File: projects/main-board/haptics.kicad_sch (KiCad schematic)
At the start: 12 parts, among them M1 Motor_DC, M2 Motor_DC, Q1 Q_NPN_CBE, Q2 Q_NPN_CBE

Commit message: Updated schematics with new symbols
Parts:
- removed U11: ~, symbol symbol-library:TLV74330PDBVR
- added U7: TLV74330PDBVR, footprint-library:TLV74330PDBVR, symbol symbol-library:TLV74330PDBVR
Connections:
- net GND: now also U7.2 (GND)
- net MOTOR_PWR_EN: now also U7.3 (EN)
- net VSYS: now also U7.1 (IN)
- net at C101.1, C103.1, M1.1 (+)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: now also U7.5 (OUT)
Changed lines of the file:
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@@
-	)
-	(symbol
-		(lib_id "symbol-library:TLV74330PDBVR")
-		(at 104.14 74.93 0)
-		(unit 1)
-		(exclude_from_sim no)
-		(in_bom yes)
-		(on_board yes)
-		(dnp no)
-		(property "Reference" "U11"
-			(at 105.664 73.66 0)
-			(effects
-				(font
-					(size 1.27 1.27)
-				)
-			)
-		)
-		(property "Value" "~"
-			(at 109.474 73.406 0)
-			(effects
-				(font
-					(size 1.27 1.27)
-				)
-			)
-		)
-		(property "Footprint" ""
-			(at 104.14 74.93 0)
-			(effects
-				(font
-					(size 1.27 1.27)
-				)
-				(hide yes)
-			)
-		)
-		(property "Datasheet" ""
-			(at 104.14 74.93 0)
-			(effects
-				(font
-					(size 1.27 1.27)
-				)
-				(hide yes)
-			)
-		)
-		(property "Description" ""
-			(at 104.14 74.93 0)
-			(effects
-				(font
-					(size 1.27 1.27)
-				)
-				(hide yes)
-			)
-		)
-		(pin "3"
-		)
-		(pin "1"
-		)
-		(pin "5"
-		)
-		(pin "4"
-		)
-		(pin "2"
-		)
-		(instances
-			(project ""
-				(path "/c621b5fd-2ef7-4a67-960d-0ffc72b1245a/ad680993-3156-41a9-bb71-e4719f61fa1c"
-					(reference "U11")
-					(unit 1)
-				)
-			)
-		)
 	)
 	(symbol
@@
 					(unit 1)
 				)
+			)
+		)
+	)
+	(symbol
+		(lib_name "TLV74330PDBVR_1")
+		(lib_id "symbol-library:TLV74330PDBVR")
+		(at 104.14 74.93 0)
+		(unit 1)
+		(exclude_from_sim no)
+		(in_bom yes)
+		(on_board yes)
+		(dnp no)
+		(property "Reference" "U7"
+			(at 105.156 73.914 0)
+			(effects
+				(font
+					(size 1.27 1.27)
+				)
+			)
+		)
+		(property "Value" "TLV74330PDBVR"
+			(at 110.998 96.774 0)
+			(effects
+				(font
+					(size 1.27 1.27)
+				)
+			)
+		)
+		(property "Footprint" "footprint-library:TLV74330PDBVR"
+			(at 117.348 97.79 0)
+			(effects
+				(font
+					(size 1.27 1.27)
+				)
+				(hide yes)
+			)
+		)
+		(property "Datasheet" ""
+			(at 104.14 74.93 0)
+			(effects
+				(font
+					(size 1.27 1.27)
+				)
+				(hide yes)
+			)
+		)
+		(property "Description" ""
+			(at 104.14 74.93 0)
+			(effects
+				(font
+					(size 1.27 1.27)
+				)
+				(hide yes)
+			)
+		)
+		(pin "1"
+		)
+		(pin "3"
+		)
+		(pin "5"
+		)
+		(pin "4"
+		)
+		(pin "2"
+		)
+		(instances
+			(project ""
+				(path "/c621b5fd-2ef7-4a67-960d-0ffc72b1245a/ad680993-3156-41a9-bb71-e4719f61fa1c"
+					(reference "U7")
+					(unit 1)
+				)

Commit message: Re-annotate schematics.
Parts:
- renumbered C99 to C101, C101 to C102, R18 to R57, R14 to R58, R17 to R59, U7 to U12
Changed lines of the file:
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@@
 		(dnp no)
 		(fields_autoplaced yes)
-		(property "Reference" "#PWR0130"
+		(property "Reference" "#PWR0145"
 			(at 77.47 92.71 0)
 			(effects
@@
 			(project "main-board"
 				(path "/c621b5fd-2ef7-4a67-960d-0ffc72b1245a/ad680993-3156-41a9-bb71-e4719f61fa1c"
-					(reference "#PWR0130")
+					(reference "#PWR0145")
 					(unit 1)
 				)
@@
 		(dnp no)
 		(fields_autoplaced yes)
-		(property "Reference" "#PWR0128"
+		(property "Reference" "#PWR0144"
 			(at 77.47 80.01 0)
 			(effects
@@
 			(project ""
 				(path "/c621b5fd-2ef7-4a67-960d-0ffc72b1245a/ad680993-3156-41a9-bb71-e4719f61fa1c"
-					(reference "#PWR0128")
+					(reference "#PWR0144")
 					(unit 1)
 				)
@@
 		(on_board yes)
 		(dnp no)
-		(property "Reference" "R18"
+		(property "Reference" "R57"
 			(at 94.488 97.282 0)
 			(effects
@@
 			(project "main-board"
 				(path "/c621b5fd-2ef7-4a67-960d-0ffc72b1245a/ad680993-3156-41a9-bb71-e4719f61fa1c"
-					(reference "R18")
+					(reference "R57")
 					(unit 1)
 				)
@@
 		(dnp no)
 		(fields_autoplaced yes)
-		(property "Reference" "#PWR0133"
+		(property "Reference" "#PWR0146"
 			(at 97.79 132.08 0)
 			(effects
@@
 			(project "main-board"
 				(path "/c621b5fd-2ef7-4a67-960d-0ffc72b1245a/ad680993-3156-41a9-bb71-e4719f61fa1c"
-					(reference "#PWR0133")
+					(reference "#PWR0146")
 					(unit 1)
 				)
@@
 		(on_board yes)
 		(dnp no)
-		(property "Reference" "R14"
+		(property "Reference" "R58"
 			(at 152.654 105.664 90)
 			(effects
@@
 			(project ""
 				(path "/c621b5fd-2ef7-4a67-960d-0ffc72b1245a/ad680993-3156-41a9-bb71-e4719f61fa1c"
-					(reference "R14")
+					(reference "R58")
 					(unit 1)
 				)
@@
 		(dnp no)
 		(fields_autoplaced yes)
-		(property "Reference" "C99"
+		(property "Reference" "C101"
 			(at 92.71 80.0162 0)
 			(effects
@@
 			(project "main-board"
 				(path "/c621b5fd-2ef7-4a67-960d-0ffc72b1245a/ad680993-3156-41a9-bb71-e4719f61fa1c"
-					(reference "C99")
+					(reference "C101")
 					(unit 1)
 				)
@@
 		(dnp no)
 		(fields_autoplaced yes)
-		(property "Reference" "C101"
+		(property "Reference" "C102"
 			(at 134.62 80.0162 0)
 			(effects
@@
 			(project "main-board"
 				(path "/c621b5fd-2ef7-4a67-960d-0ffc72b1245a/ad680993-3156-41a9-bb71-e4719f61fa1c"
-					(reference "C101")
+					(reference "C102")
 					(unit 1)
 				)
@@
 		(on_board yes)
 		(dnp no)
-		(property "Reference" "R17"
+		(property "Reference" "R59"
 			(at 199.39 105.918 90)
 			(effects
@@
 			(project "main-board"
 				(path "/c621b5fd-2ef7-4a67-960d-0ffc72b1245a/ad680993-3156-41a9-bb71-e4719f61fa1c"
-					(reference "R17")
+					(reference "R59")
 					(unit 1)
 				)
@@
 		(on_board yes)
 		(dnp no)
-		(property "Reference" "U7"
+		(property "Reference" "U12"
 			(at 105.156 73.914 0)
 			(effects
@@
 			(project ""
 				(path "/c621b5fd-2ef7-4a67-960d-0ffc72b1245a/ad680993-3156-41a9-bb71-e4719f61fa1c"
-					(reference "U7")
-					(unit 1)
-				)
+					(reference "U12")
+					(unit 1)
+				)

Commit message: Normalise capacitors
- Add capacitor parts to library.
- Replace all placeholder capacitors
  with the actual part numbers.
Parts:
- removed C100, C102: 10uF 10V, symbol Device:C_Small
- removed C101, C103: 100nF 10V, symbol Device:C_Small
- added C100, C102: 10uF 10V, Capacitor_SMD:C_0603_1608Metric, symbol symbol-library-capacitors:CC0603MRX5R6BB106
- added C101, C103: 100nF 10V, Capacitor_SMD:C_0402_1005Metric, symbol symbol-library-capacitors:CC0402KRX7R6BB104
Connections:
- net GND: now also C100.2, C101.2, C102.2, C103.2
- net VSYS: now also C100.1, C101.1
- net at M1.1 (+), M2.1 (+), U12.5 (OUT): now also C102.1, C103.1

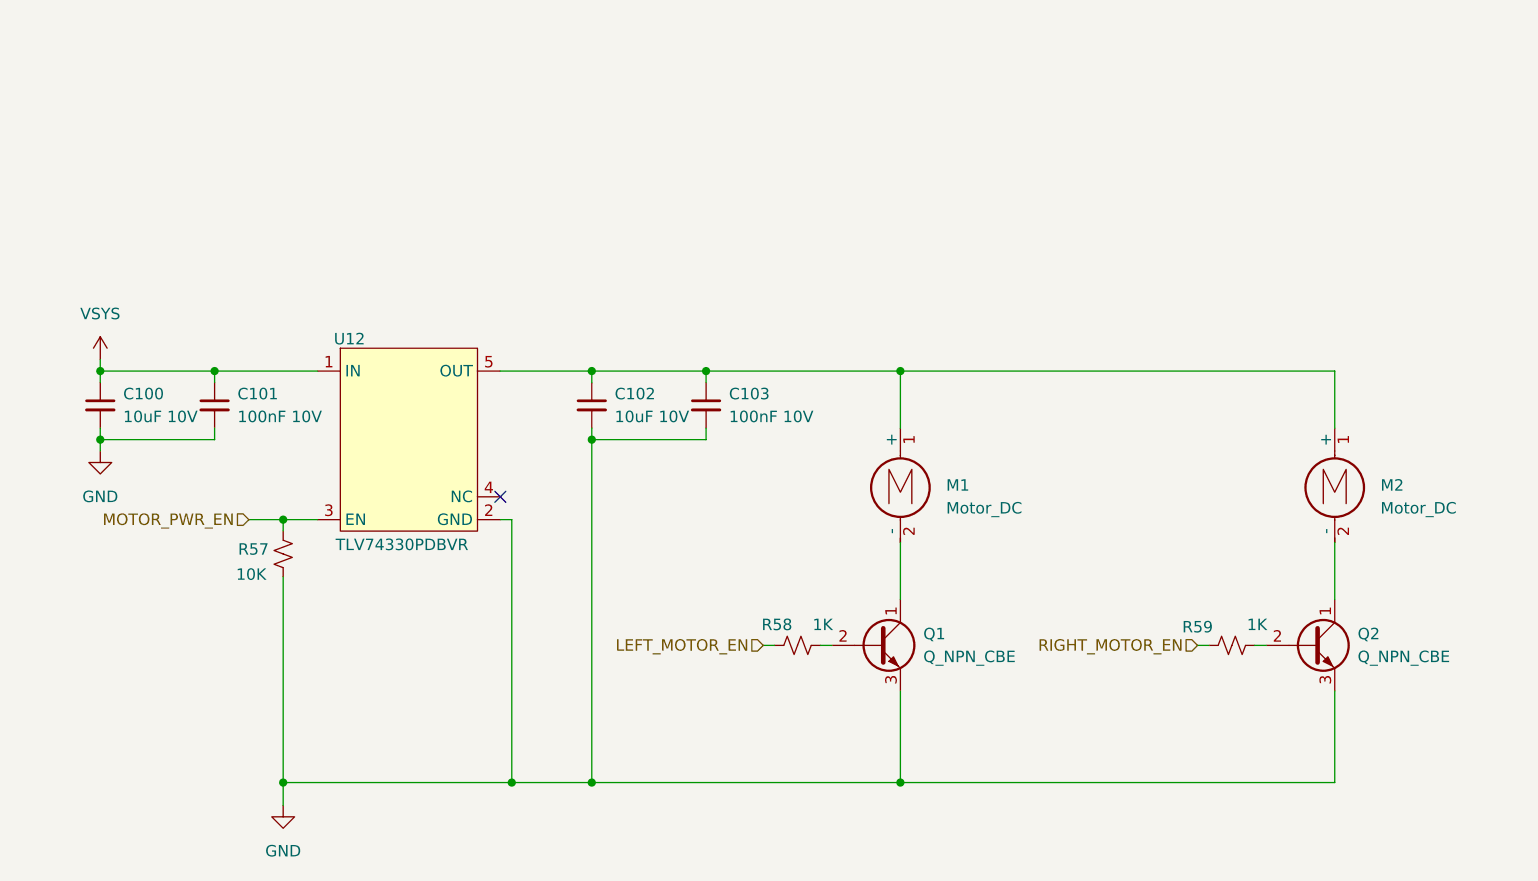
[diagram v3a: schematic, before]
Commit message: Replace placeholder resistors
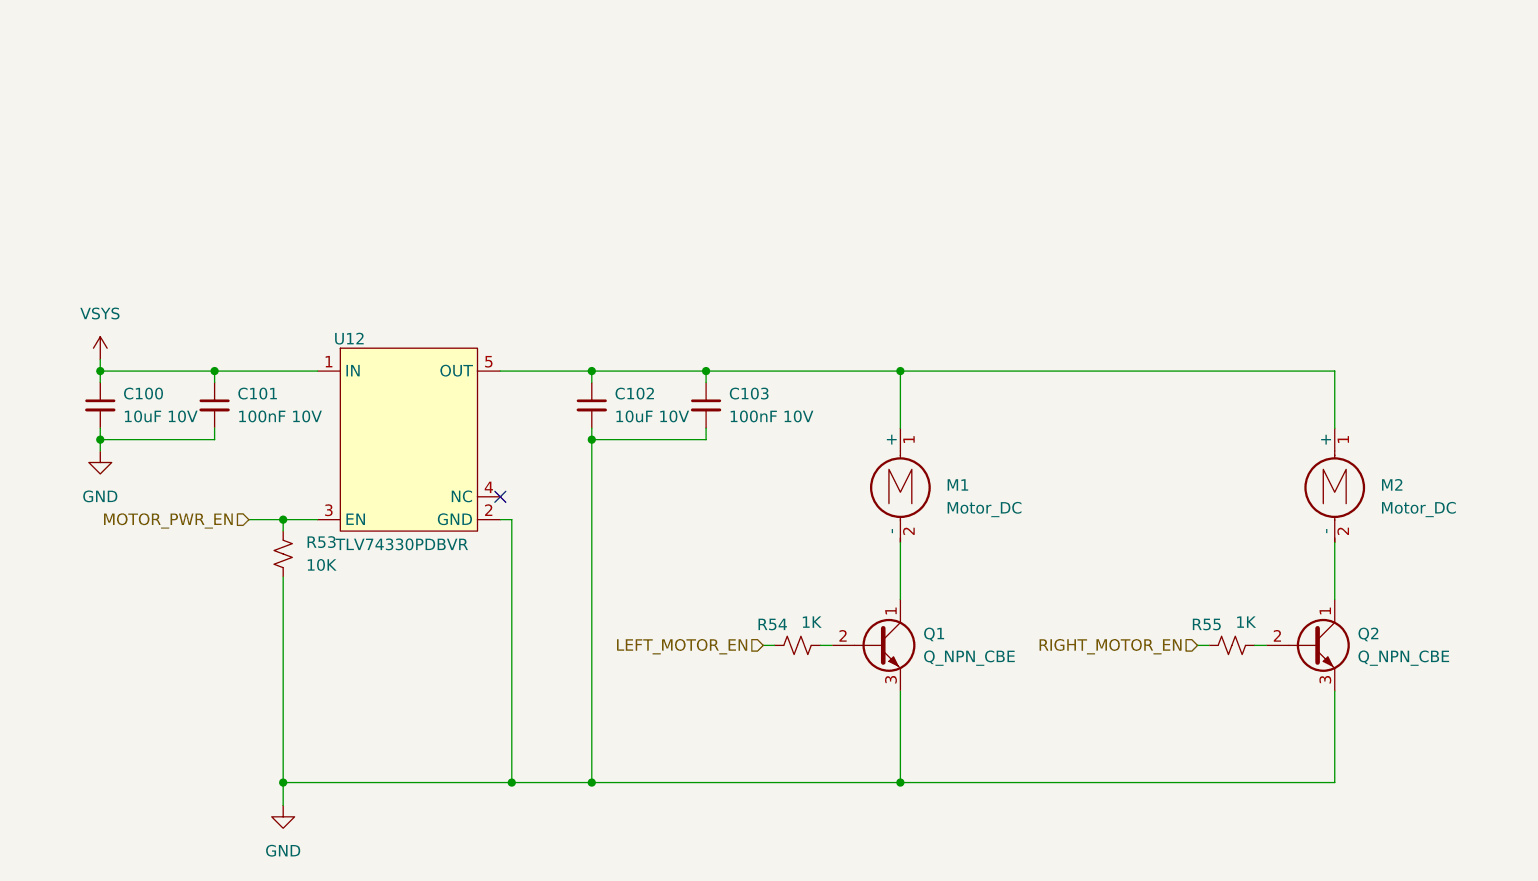
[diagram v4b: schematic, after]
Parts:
- removed R57: 10K, symbol Device:R_Small_US
- removed R58, R59: 1K, symbol Device:R_Small_US
- added R53: 10K, Resistor_SMD:R_0402_1005Metric, symbol symbol-library-resistors:RC0402JR-0710KL
- added R54, R55: 1K, Resistor_SMD:R_0402_1005Metric, symbol symbol-library-resistors:RC0402JR-071KL
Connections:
- net GND: now also R53.2
- net LEFT_MOTOR_EN: now also R54.1
- net MOTOR_PWR_EN: now also R53.1
- net RIGHT_MOTOR_EN: now also R55.1
- net at Q1.2 (B): now also R54.2
- net at Q2.2 (B): now also R55.2
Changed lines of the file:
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@@
-	)
-	(symbol
-		(lib_id "Device:R_Small_US")
-		(at 97.79 97.79 180)
-		(unit 1)
-		(exclude_from_sim no)
-		(in_bom yes)
-		(on_board yes)
-		(dnp no)
-		(property "Reference" "R57"
-			(at 94.488 97.282 0)
-			(effects
-				(font
-					(size 1.27 1.27)
-				)
-			)
-		)
-		(property "Value" "10K"
-			(at 94.234 100.076 0)
-			(effects
-				(font
-					(size 1.27 1.27)
-				)
-			)
-		)
-		(property "Footprint" ""
-			(at 97.79 97.79 0)
-			(effects
-				(font
-					(size 1.27 1.27)
-				)
-				(hide yes)
-			)
-		)
-		(property "Datasheet" "~"
-			(at 97.79 97.79 0)
-			(effects
-				(font
-					(size 1.27 1.27)
-				)
-				(hide yes)
-			)
-		)
-		(property "Description" "Resistor, small US symbol"
-			(at 97.79 97.79 0)
-			(effects
-				(font
-					(size 1.27 1.27)
-				)
-				(hide yes)
-			)
-		)
-		(pin "2"
-		)
-		(pin "1"
-		)
-		(instances
-			(project "main-board"
-				(path "/c621b5fd-2ef7-4a67-960d-0ffc72b1245a/ad680993-3156-41a9-bb71-e4719f61fa1c"
-					(reference "R57")
-					(unit 1)
-				)
-			)
-		)
 	)
 	(symbol
@@
 	)
 	(symbol
-		(lib_id "Device:R_Small_US")
-		(at 154.94 107.95 90)
-		(unit 1)
-		(exclude_from_sim no)
-		(in_bom yes)
-		(on_board yes)
-		(dnp no)
-		(property "Reference" "R58"
-			(at 152.654 105.664 90)
-			(effects
-				(font
-					(size 1.27 1.27)
-				)
-			)
-		)
-		(property "Value" "1K"
-			(at 157.734 105.664 90)
-			(effects
-				(font
-					(size 1.27 1.27)
-				)
-			)
-		)
-		(property "Footprint" ""
-			(at 154.94 107.95 0)
-			(effects
-				(font
-					(size 1.27 1.27)
-				)
-				(hide yes)
-			)
-		)
-		(property "Datasheet" "~"
-			(at 154.94 107.95 0)
+		(lib_id "symbol-library-resistors:RC0402JR-0710KL")
+		(at 97.79 97.79 0)
+		(unit 1)
+		(exclude_from_sim no)
+		(in_bom yes)
+		(on_board yes)
+		(dnp no)
+		(fields_autoplaced yes)
+		(property "Reference" "R53"
+			(at 100.33 96.5199 0)
+			(effects
+				(font
+					(size 1.27 1.27)
+				)
+				(justify left)
+			)
+		)
+		(property "Value" "10K"
+			(at 100.33 99.0599 0)
+			(effects
+				(font
+					(size 1.27 1.27)
+				)
+				(justify left)
+			)
+		)
+		(property "Footprint" "Resistor_SMD:R_0402_1005Metric"
+			(at 97.79 97.79 0)
+			(effects
+				(font
+					(size 1.27 1.27)
+				)
+				(hide yes)
+			)
+		)
+		(property "Datasheet" "~"
+			(at 97.79 97.79 0)
 			(effects
 				(font
@@
 		)
 		(property "Description" "Resistor, small US symbol"
-			(at 154.94 107.95 0)
-			(effects
-				(font
-					(size 1.27 1.27)
-				)
-				(hide yes)
-			)
-		)
-		(pin "2"
-		)
-		(pin "1"
-		)
-		(instances
-			(project ""
-				(path "/c621b5fd-2ef7-4a67-960d-0ffc72b1245a/ad680993-3156-41a9-bb71-e4719f61fa1c"
-					(reference "R58")
+			(at 97.79 97.79 0)
+			(effects
+				(font
+					(size 1.27 1.27)
+				)
+				(hide yes)
+			)
+		)
+		(pin "1"
+		)
+		(pin "2"
+		)
+		(instances
+			(project "main-board"
+				(path "/c621b5fd-2ef7-4a67-960d-0ffc72b1245a/ad680993-3156-41a9-bb71-e4719f61fa1c"
+					(reference "R53")
 					(unit 1)
 				)
@@
 	)
 	(symbol
+		(lib_id "symbol-library-resistors:RC0402JR-071KL")
+		(at 203.2 107.95 90)
+		(unit 1)
+		(exclude_from_sim no)
+		(in_bom yes)
+		(on_board yes)
+		(dnp no)
+		(property "Reference" "R55"
+			(at 200.406 105.664 90)
+			(effects
+				(font
+					(size 1.27 1.27)
+				)
+			)
+		)
+		(property "Value" "1K"
+			(at 204.724 105.41 90)
+			(effects
+				(font
+					(size 1.27 1.27)
+				)
+			)
+		)
+		(property "Footprint" "Resistor_SMD:R_0402_1005Metric"
+			(at 203.2 107.95 0)
+			(effects
+				(font
+					(size 1.27 1.27)
+				)
+				(hide yes)
+			)
+		)
+		(property "Datasheet" "~"
+			(at 203.2 107.95 0)
+			(effects
+				(font
+					(size 1.27 1.27)
+				)
+				(hide yes)
+			)
+		)
+		(property "Description" "Resistor, small US symbol"
+			(at 203.2 107.95 0)
+			(effects
+				(font
+					(size 1.27 1.27)
+				)
+				(hide yes)
+			)
+		)
+		(pin "1"
+		)
+		(pin "2"
+		)
+		(instances
+			(project "main-board"
+				(path "/c621b5fd-2ef7-4a67-960d-0ffc72b1245a/ad680993-3156-41a9-bb71-e4719f61fa1c"
+					(reference "R55")
+					(unit 1)
+				)
+			)
+		)
+	)
+	(symbol
+		(lib_id "symbol-library-resistors:RC0402JR-071KL")
+		(at 154.94 107.95 90)
+		(unit 1)
+		(exclude_from_sim no)
+		(in_bom yes)
+		(on_board yes)
+		(dnp no)
+		(property "Reference" "R54"
+			(at 152.146 105.664 90)
+			(effects
+				(font
+					(size 1.27 1.27)
+				)
+			)
+		)
+		(property "Value" "1K"
+			(at 156.464 105.41 90)
+			(effects
+				(font
+					(size 1.27 1.27)
+				)
+			)
+		)
+		(property "Footprint" "Resistor_SMD:R_0402_1005Metric"
+			(at 154.94 107.95 0)
+			(effects
+				(font
+					(size 1.27 1.27)
+				)
+				(hide yes)
+			)
+		)
+		(property "Datasheet" "~"
+			(at 154.94 107.95 0)
+			(effects
+				(font
+					(size 1.27 1.27)
+				)
+				(hide yes)
+			)
+		)
+		(property "Description" "Resistor, small US symbol"
+			(at 154.94 107.95 0)
+			(effects
+				(font
+					(size 1.27 1.27)
+				)
+				(hide yes)
+			)
+		)
+		(pin "1"
+		)
+		(pin "2"
+		)
+		(instances
+			(project ""
+				(path "/c621b5fd-2ef7-4a67-960d-0ffc72b1245a/ad680993-3156-41a9-bb71-e4719f61fa1c"
+					(reference "R54")
+					(unit 1)
+				)
+			)
+		)
+	)
+	(symbol
 		(lib_id "symbol-library-capacitors:CC0402KRX7R6BB104")
 		(at 90.17 81.28 0)
@@
 					(unit 1)
 				)
-			)
-		)
-	)
-	(symbol
-		(lib_id "Device:R_Small_US")
-		(at 203.2 107.95 90)
-		(unit 1)
-		(exclude_from_sim no)
-		(in_bom yes)
-		(on_board yes)
-		(dnp no)
-		(property "Reference" "R59"
-			(at 199.39 105.918 90)
-			(effects
-				(font
-					(size 1.27 1.27)
-				)
-			)
-		)
-		(property "Value" "1K"
-			(at 205.994 105.664 90)
-			(effects
-				(font
-					(size 1.27 1.27)
-				)
-			)
-		)
-		(property "Footprint" ""
-			(at 203.2 107.95 0)
-			(effects
-				(font
-					(size 1.27 1.27)
-				)
-				(hide yes)
-			)
-		)
-		(property "Datasheet" "~"
-			(at 203.2 107.95 0)
-			(effects
-				(font
-					(size 1.27 1.27)
-				)
-				(hide yes)
-			)
-		)
-		(property "Description" "Resistor, small US symbol"
-			(at 203.2 107.95 0)
-			(effects
-				(font
-					(size 1.27 1.27)
-				)
-				(hide yes)
-			)
-		)
-		(pin "2"
-		)
-		(pin "1"
-		)
-		(instances
-			(project "main-board"
-				(path "/c621b5fd-2ef7-4a67-960d-0ffc72b1245a/ad680993-3156-41a9-bb71-e4719f61fa1c"
-					(reference "R59")
-					(unit 1)
-				)

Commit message: Add footprints
- Inductors
- Switches
- Buttons
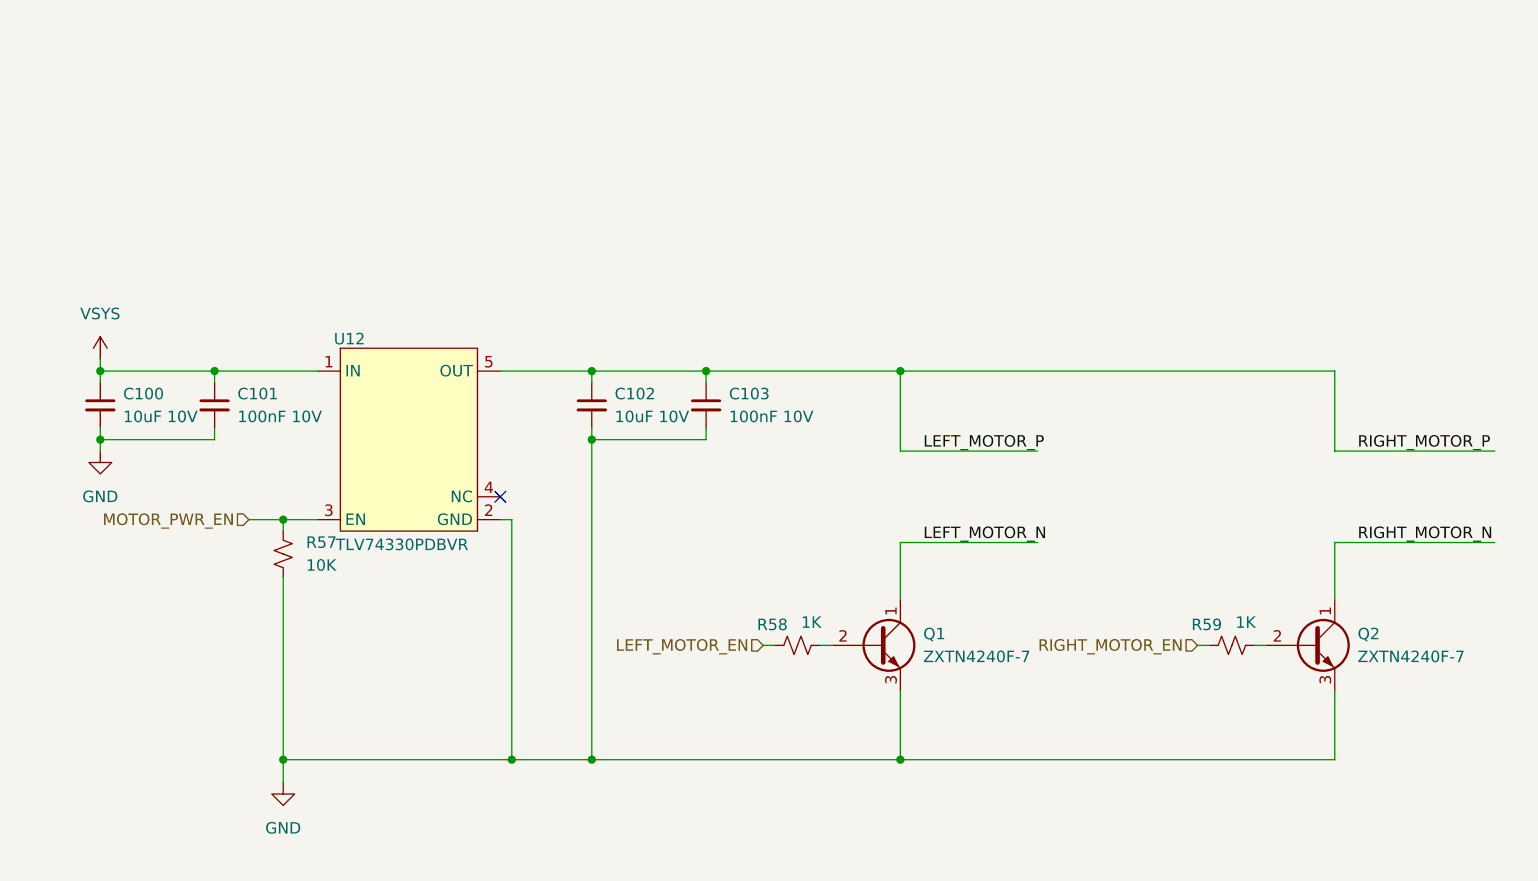
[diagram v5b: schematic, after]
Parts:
- removed M1, M2: Motor_DC, symbol Motor:Motor_DC
- removed Q1, Q2: Q_NPN_CBE, symbol Transistor_BJT:Q_NPN_CBE
- added Q1, Q2: ZXTN4240F-7, footprint-library:SOT23_ZXTN_DIO, symbol symbol-library-transistors:ZXTN4240F-7
- renumbered R53 to R57, R54 to R58, R55 to R59
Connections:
- net GND: now also Q1.3 (E), Q2.3 (E)
- net LEFT_MOTOR_P: now reaches C102.1, C103.1, U12.5 (OUT)
- net at R58.2: now also Q1.2 (B)
- net at R59.2: now also Q2.2 (B)
- new net LEFT_MOTOR_N: Q1.1 (C)
- new net RIGHT_MOTOR_N: Q2.1 (C)
